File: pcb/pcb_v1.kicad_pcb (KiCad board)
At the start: 2 copper layers, 95.9 x 90.2 mm, 51 parts, among them IC1 MPU-9250, J1 CONN_01X10, J2 CONN_01X02, U1 ISA_BUS_connector, U2 MSP432P4111, U3 LM317_SOT223, U4 STWD100, U5 ACS711, U6 MCP9701T-E/TTCT-ND, U7 FM25V05, U8 ST1W008S4ER, Y1 32kHz, Y2 48MHz

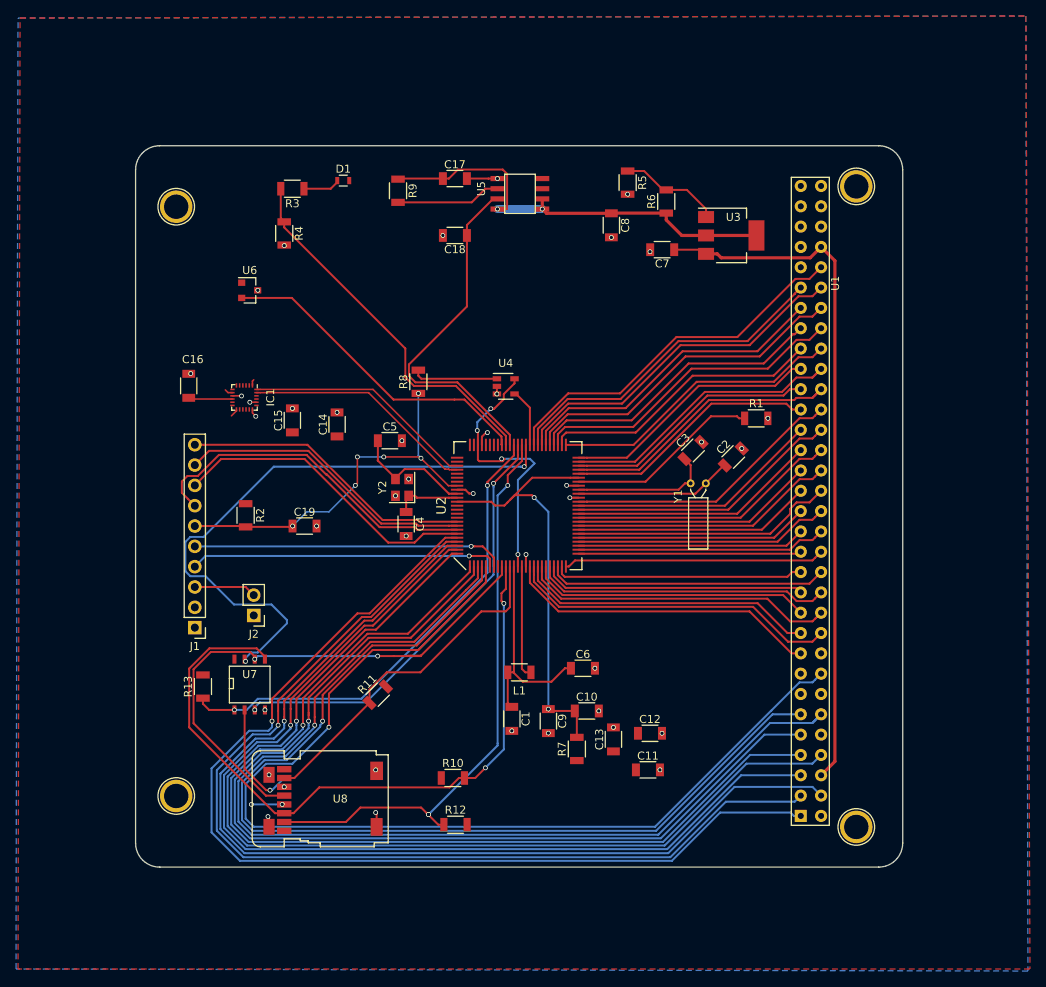
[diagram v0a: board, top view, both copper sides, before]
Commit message: add logo in the PCB
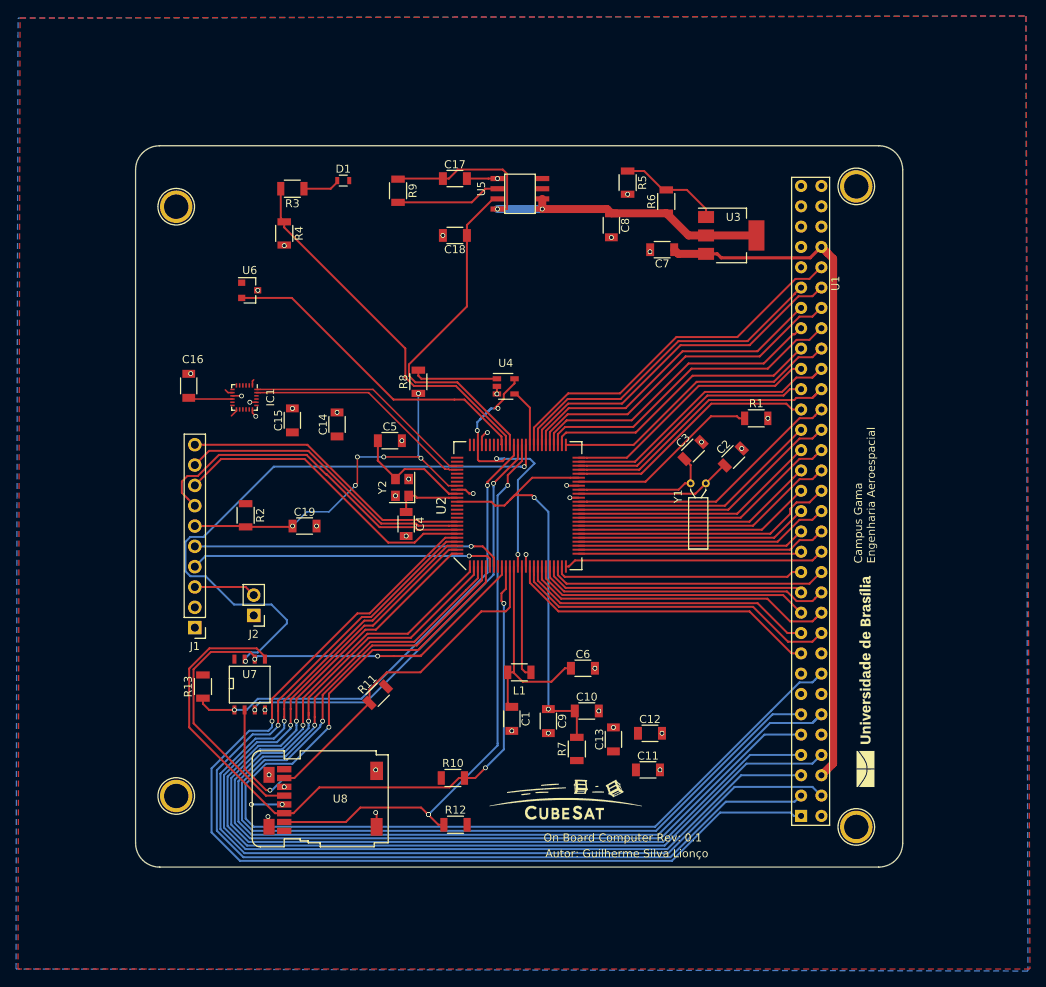
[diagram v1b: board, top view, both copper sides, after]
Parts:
- added G***: LOGO, footprint:cubesat_logo, F.Cu at (103.8, 132.3)
- added G***: LOGO, footprint:unb_logo_pb, F.Cu at (141.2, 117.0)
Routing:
- net +5V: track 88.3 -> 155.6 mm
- net /3v3_ACS: track 40.7 -> 45.2 mm
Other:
- board text added: "Autor: Guilherme Silva Lionço"
- board text added: "Campus Gama Engenharia Aeroespacial"
- board text added: "On Board Computer Rev: 0.1"

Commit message: add flowcharts
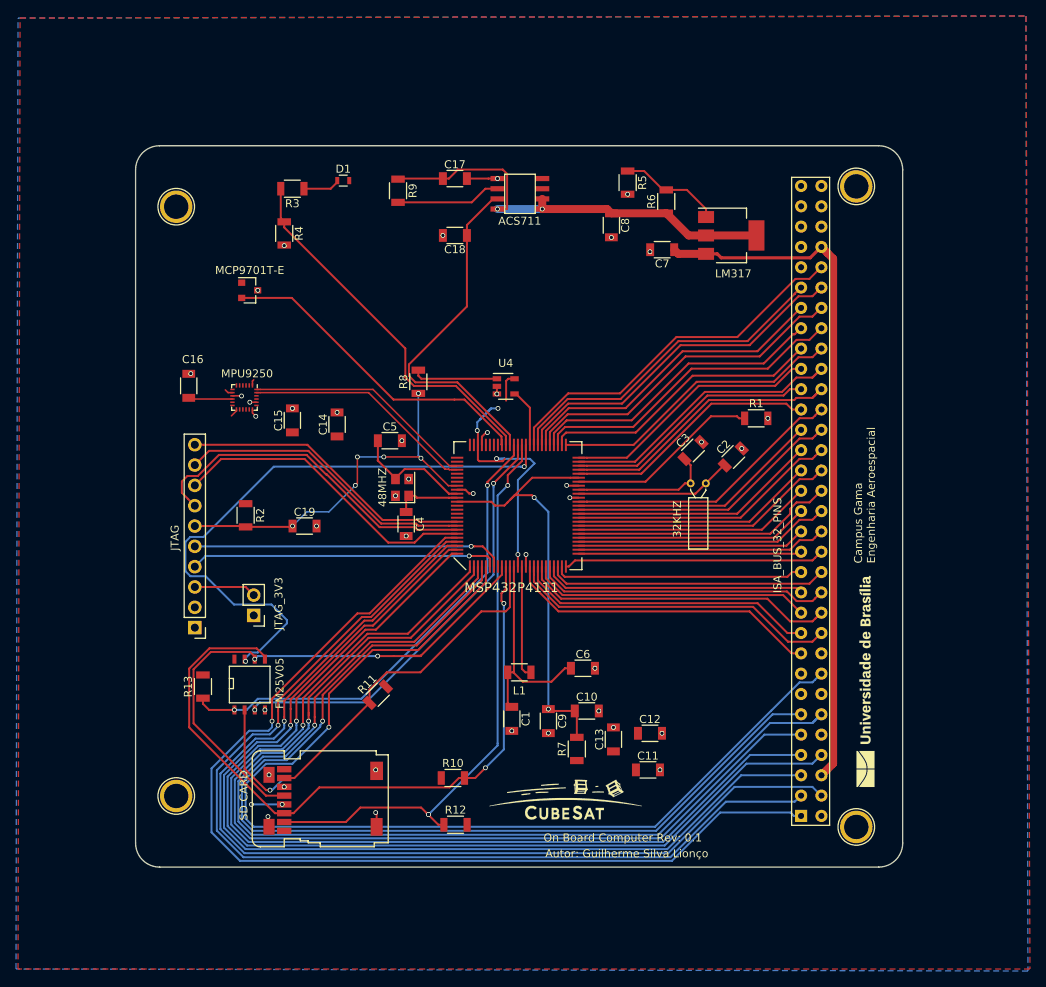
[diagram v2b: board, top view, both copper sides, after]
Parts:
- SD CARD: renamed from U8
- renumbered Y1 to 32KHZ, Y2 to 48MHZ, U5 to ACS711, U7 to FM25V05, U1 to ISA_BUS_32_PINS, J1 to JTAG, J2 to JTAG_3V3, U3 to LM317, U6 to MCP9701T-E, IC1 to MPU9250, U2 to MSP432P4111
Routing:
- net /3v3_ACS: track 45.2 -> 44.0 mm
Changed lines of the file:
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@@
   (general
     (thickness 1.6)
-    (drawings 28)
-    (tracks 836)
+    (drawings 27)
+    (tracks 835)
     (zones 0)
     (modules 53)
@@
   (page A4)
   (layers
-    (0 F.Cu signal hide)
-    (31 B.Cu signal hide)
+    (0 F.Cu signal)
+    (31 B.Cu signal)
     (32 B.Adhes user hide)
     (33 F.Adhes user hide)
     (34 B.Paste user hide)
     (35 F.Paste user hide)
-    (36 B.SilkS user hide)
+    (36 B.SilkS user)
     (37 F.SilkS user)
-    (38 B.Mask user hide)
+    (38 B.Mask user)
     (39 F.Mask user)
     (40 Dwgs.User user hide)
-    (41 Cmts.User user)
+    (41 Cmts.User user hide)
     (42 Eco1.User user hide)
     (43 Eco2.User user hide)
@@
     (visible_elements 7FFFFFFF)
     (pcbplotparams
-      (layerselection 0x010b0_ffffffff)
+      (layerselection 0x010f0_ffffffff)
       (usegerberextensions true)
       (usegerberattributes false)
@@
       (padsonsilk false)
       (subtractmaskfromsilk false)
-      (outputformat 4)
+      (outputformat 1)
       (mirror false)
       (drillshape 0)
       (scaleselection 1)
-      (outputdirectory "layout"))
+      (outputdirectory "gerbers"))
   )
   (net 0 "")
@@
     (descr "Crystal THT DS26 6.0mm length 2.0mm diameter http://www.microcrystal.com/images/_Product-Documentation/03_TF_metal_Packages/01_Datasheet/DS-Series.pdf")
     (tags ['DS26'])
-    (fp_text reference Y1 (at -1.57 1.625 270) (layer F.SilkS)
+    (fp_text reference 32KHZ (at -1.6764 4.4704 90) (layer F.SilkS)
       (effects (font (size 1 1) (thickness 0.15)))
     )
@@
   (module PCB_TCC:MSP432P4111 (layer F.Cu)
     (at 97.79 94.996 90)
-    (fp_text reference U2 (at 0 -9.575 90) (layer F.SilkS)
+    (fp_text reference MSP432P4111 (at -10.2362 -0.8128 180) (layer F.SilkS)
       (effects (font (size 1.2 1.2) (thickness 0.15)))
     )
@@
   (module ".pretty:ACS711_8-pin SOICN" (layer F.Cu)
     (at 100.838 57.912 90)
-    (fp_text reference U5 (at 2.54 -7.62 90) (layer F.SilkS)
+    (fp_text reference ACS711 (at -1.4986 -2.8194 180) (layer F.SilkS)
       (effects (font (size 1 1) (thickness 0.15)))
     )
@@
     (tags "CMS SOT")
     (attr smd)
-    (fp_text reference U3 (at 0.254 -2.286) (layer F.SilkS)
+    (fp_text reference LM317 (at 0.254 4.7752) (layer F.SilkS)
       (effects (font (size 1 1) (thickness 0.15)))
     )
@@
   (module isaConnector:ISA_CONNECTOR (layer F.Cu)
     (at 130.65 126.15 90)
-    (fp_text reference U1 (at 58.95364 6.8557 90) (layer F.SilkS)
+    (fp_text reference ISA_BUS_32_PINS (at 26.201 -0.3988 90) (layer F.SilkS)
       (effects (font (size 1 1) (thickness 0.15)))
     )
@@
     (descr "Through hole straight pin header, 1x10, 2.54mm pitch, single row")
     (tags "Through hole pin header THT 1x10 2.54mm single row")
-    (fp_text reference J1 (at 0 -2.33) (layer F.SilkS)
+    (fp_text reference JTAG (at 2.4892 11.2268 270) (layer F.SilkS)
       (effects (font (size 1 1) (thickness 0.15)))
     )
@@
     (descr "Through hole straight pin header, 1x02, 2.54mm pitch, single row")
     (tags "Through hole pin header THT 1x02 2.54mm single row")
-    (fp_text reference J2 (at 0 -2.33) (layer F.SilkS)
+    (fp_text reference JTAG_3V3 (at -3.1242 1.4732 270) (layer F.SilkS)
       (effects (font (size 1 1) (thickness 0.15)))
     )
@@
     (tags SOT-23)
     (attr smd)
-    (fp_text reference U6 (at 0 -2.5) (layer F.SilkS)
+    (fp_text reference MCP9701T-E (at 0 -2.5) (layer F.SilkS)
       (effects (font (size 1 1) (thickness 0.15)))
     )
@@
     (tags "CMS SOJ")
     (attr smd)
-    (fp_text reference U7 (at 0 -1.27) (layer F.SilkS)
+    (fp_text reference FM25V05 (at 3.7592 -0.1524 90) (layer F.SilkS)
       (effects (font (size 1 1) (thickness 0.15)))
     )
@@
     (tags "SMD SMT crystal oscillator")
     (attr smd)
-    (fp_text reference Y2 (at 0 -2.45 270) (layer F.SilkS)
+    (fp_text reference 48MHZ (at 0 -2.45 90) (layer F.SilkS)
       (effects (font (size 1 1) (thickness 0.15)))
     )
@@
   (module ST1W008S4ER1500:ST1W008S4ER1500 (layer F.Cu)
     (at 68.58 135.636)
-    (fp_text reference U8 (at 7 -4) (layer F.SilkS)
+    (fp_text reference "SD CARD" (at -5.0546 -4.4196 90) (layer F.SilkS)
       (effects (font (size 1 1) (thickness 0.15)))
     )
@@
     (tags "QFN 0.4")
     (attr smd)
-    (fp_text reference IC1 (at 0 -3.25 90) (layer F.SilkS)
+    (fp_text reference MPU9250 (at -2.975 -0.3238 180) (layer F.SilkS)
       (effects (font (size 1 1) (thickness 0.15)))
     )
@@
     (arrow2b (pts (xy 50.154127 43.596006) (xy 51.282182 43.012575)))
   )
-  (target plus (at 50.038 140.208) (size 5) (width 0.15) (layer Edge.Cuts))
   (via (at 80.01 133.35) (size 0.6) (drill 0.4) (layers F.Cu B.Cu) (net 0))
   (segment (start 80.13 133.47) (end 80.01 133.35) (width 0.25) (layer F.Cu) (net 0))
@@
   (via (at 64.481087 132.334) (size 0.6) (drill 0.4) (layers F.Cu B.Cu) (net 8))
   (segment (start 67.564 132.334) (end 64.481087 132.334) (width 0.25) (layer B.Cu) (net 8))
-  (segment (start 96.021001 81.673814) (end 94.827401 82.867414) (width 0.25) (layer F.Cu) (net 8))
   (via (at 95.3008 82.8294) (size 0.6) (drill 0.4) (layers F.Cu B.Cu) (net 8))
-  (segment (start 96.021001 81.045999) (end 96.021001 81.673814) (width 0.25) (layer F.Cu) (net 8))
-  (segment (start 97.366 79.126) (end 97.366 79.701) (width 0.25) (layer F.Cu) (net 8) (status 10))
-  (segment (start 97.366 79.701) (end 96.021001 81.045999) (width 0.25) (layer F.Cu) (net 8))
   (segment (start 96.161342 89.133938) (end 95.758 89.133938) (width 0.25) (layer B.Cu) (net 8))
   (segment (start 96.14128 89.154) (end 95.123 89.154) (width 0.25) (layer B.Cu) (net 8))
@@
   (segment (start 92.71 84.56055) (end 93.080276 84.190276) (width 0.25) (layer B.Cu) (net 8))
   (segment (start 93.080276 84.190276) (end 94.103138 83.167413) (width 0.25) (layer B.Cu) (net 8))
+  (segment (start 96.586 79.126) (end 96.3168 79.3952) (width 0.25) (layer F.Cu) (net 8))
+  (segment (start 97.366 79.126) (end 96.586 79.126) (width 0.25) (layer F.Cu) (net 8))
+  (segment (start 96.3168 79.3952) (end 96.3168 81.8642) (width 0.25) (layer F.Cu) (net 8))
   (segment (start 98.72 115.824) (end 99.42 115.824) (width 0.25) (layer F.Cu) (net 9) (status 20))
   (segment (start 98.29 115.394) (end 98.72 115.824) (width 0.25) (layer F.Cu) (net 9))

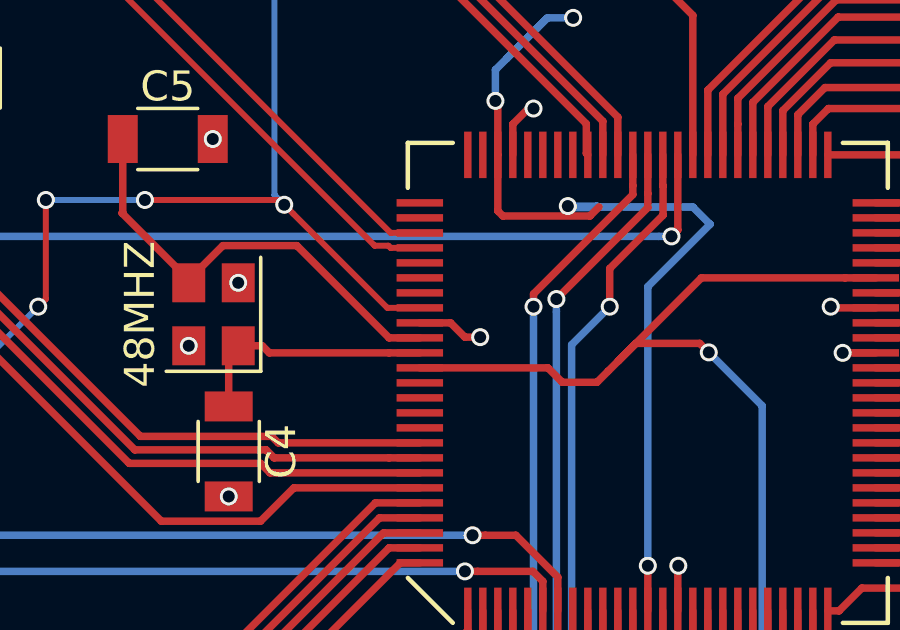
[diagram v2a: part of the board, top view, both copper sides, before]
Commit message: update CSS
Operations Mode + UML +State Machine
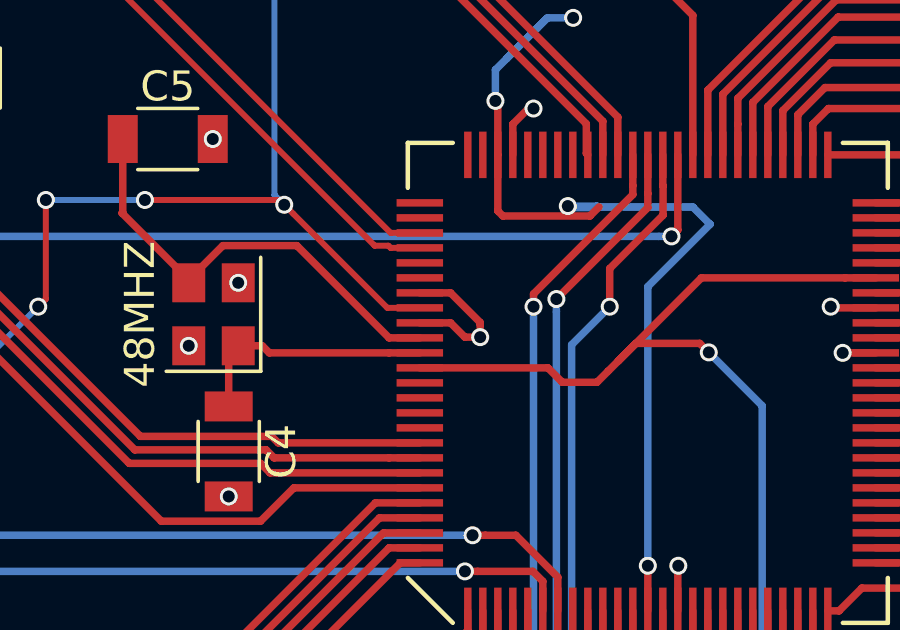
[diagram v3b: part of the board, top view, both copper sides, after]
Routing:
- net GND: track 17.9 -> 20.8 mm
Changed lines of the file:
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@@
     (thickness 1.6)
     (drawings 27)
-    (tracks 835)
+    (tracks 839)
     (zones 0)
     (modules 53)
@@
   (via (at 93.98 85.852) (size 0.6) (drill 0.4) (layers F.Cu B.Cu) (net 2))
   (segment (start 93.809 85.852) (end 93.98 85.852) (width 0.25) (layer F.Cu) (net 2))
+  (segment (start 92.202 93.047736) (end 92.202 93.472) (width 0.25) (layer F.Cu) (net 2))
+  (segment (start 92.202 92.983) (end 92.202 93.047736) (width 0.25) (layer F.Cu) (net 2))
+  (segment (start 91.215 91.996) (end 92.202 92.983) (width 0.25) (layer F.Cu) (net 2))
+  (segment (start 90.19 91.996) (end 91.215 91.996) (width 0.25) (layer F.Cu) (net 2))
   (segment (start 123.52134 89.96066) (end 123.65334 89.96066) (width 0.25) (layer F.Cu) (net 3) (status 30))
   (segment (start 121.28 92.202) (end 123.52134 89.96066) (width 0.25) (layer F.Cu) (net 3) (status 30))
